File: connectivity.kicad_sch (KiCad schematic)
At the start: 4 parts

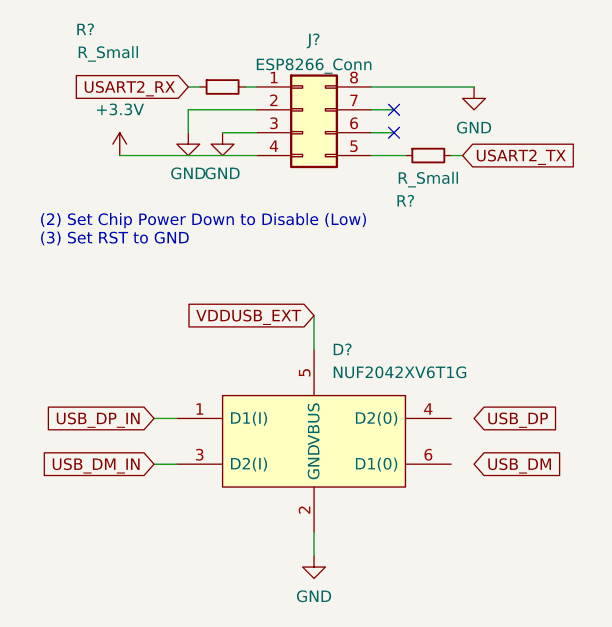
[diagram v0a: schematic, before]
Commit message: Supply: - Added voltage regulator - appended calculations for L and Voltage divider - Added USB-C connector symbol and connected D+/D- lines
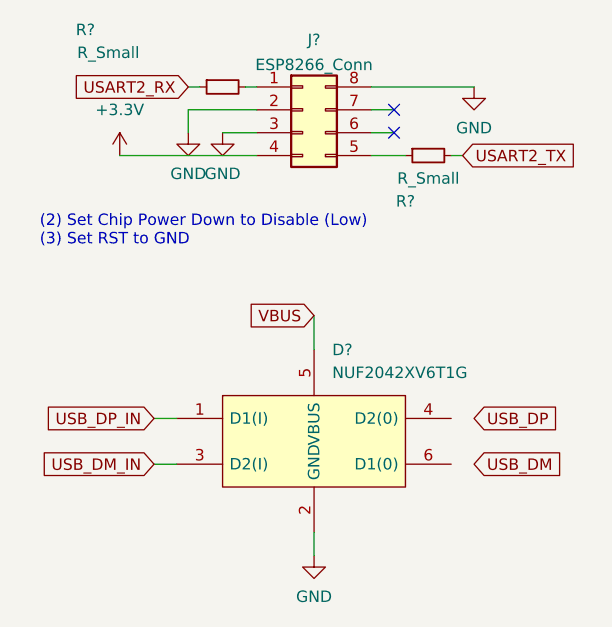
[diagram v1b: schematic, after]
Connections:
- net VDDUSB_EXT renamed VBUS
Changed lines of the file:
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@@
     )
   )
-  (global_label "VDDUSB_EXT" (shape input) (at 45.72 46.99 180) (fields_autoplaced)
+  (global_label "VBUS" (shape input) (at 45.72 46.99 180) (fields_autoplaced)
     (effects (font (size 1.27 1.27)) (justify right))
     (property "Intersheet References" "${INTERSHEET_REFS}" (id 0) (at 31.6634 46.9106 0)
